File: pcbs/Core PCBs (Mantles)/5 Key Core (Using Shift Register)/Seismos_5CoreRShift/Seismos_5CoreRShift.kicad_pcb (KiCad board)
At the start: 2 copper layers, 147 x 78 mm, 32 parts, among them IC1 74HC595, J1 SM010B-SRSS-TB(LF)(SN), J10 SM10B-SRSS-TB_(LF)(SN), J2 SM010B-SRSS-TB(LF)(SN), J3 SM010B-SRSS-TB(LF)(SN), J4 SM010B-SRSS-TB(LF)(SN), J5 SM010B-SRSS-TB(LF)(SN), J6 SM010B-SRSS-TB(LF)(SN), J7 SM09B-SRSS-TB(LF)(SN), J8 MJ-4PP-9-Lily58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

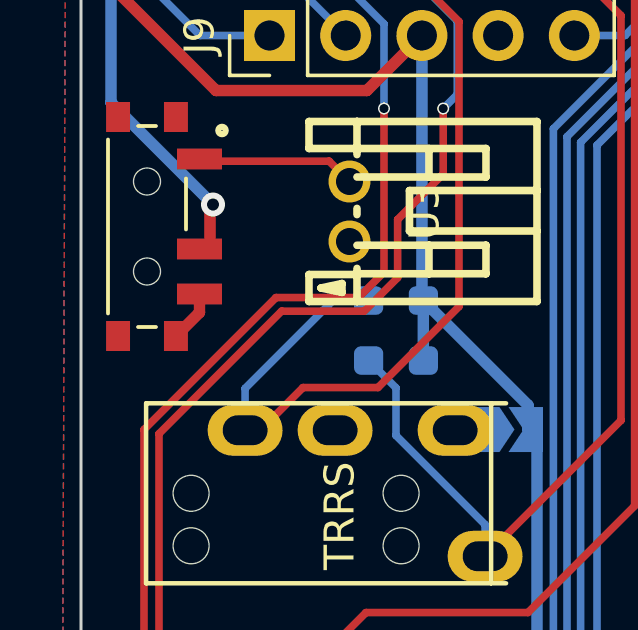
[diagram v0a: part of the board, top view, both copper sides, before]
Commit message: HOTFIX, power switch bridges to ground
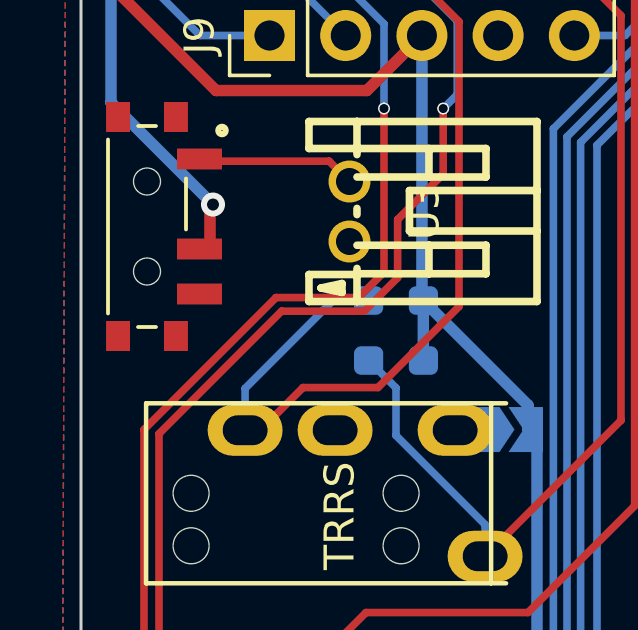
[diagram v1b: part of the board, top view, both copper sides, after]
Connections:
- U2 pad L1: GND -> unconnected-(U2-PadL1)
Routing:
- net GND: track 271.8 -> 270.0 mm

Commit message: Update PCB version and gerbers for HOTFIX
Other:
- board text added: "Rev. 2.1.0"
- board text removed: "Rev. 2.0.0"
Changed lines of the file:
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@@
 		(layer "Edge.Cuts")
 	)
-	(gr_text "Rev. 2.0.0"
+	(gr_text "Rev. 2.1.0"
 		(at 53.45 78.9 90)
 		(layer "B.SilkS")
